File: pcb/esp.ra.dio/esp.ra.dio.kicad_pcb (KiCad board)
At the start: 2 copper layers, 75 x 28 mm, 34 parts, among them J1 A, J10 UART, J2 B, J3 C, J4 D, J5 START, J6 SELECT, J7 JOY, J8 USB_B_Micro, J9 BATTERY, Q1 BSS138, SW1 POWER, SW2 RESET, SW3 BOOT, U2 VCC, U3 RT9080-33GJ5

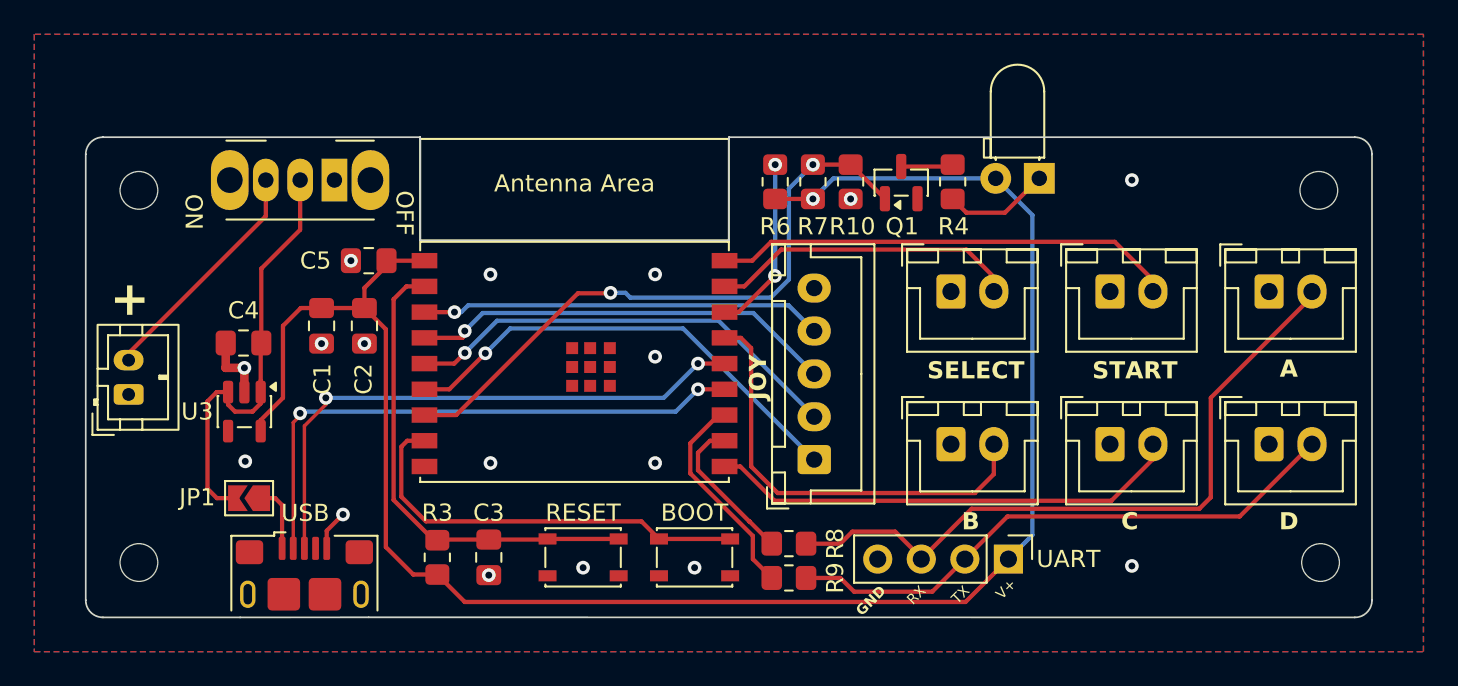
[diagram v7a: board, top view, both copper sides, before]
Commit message: Get rid of USB R0s
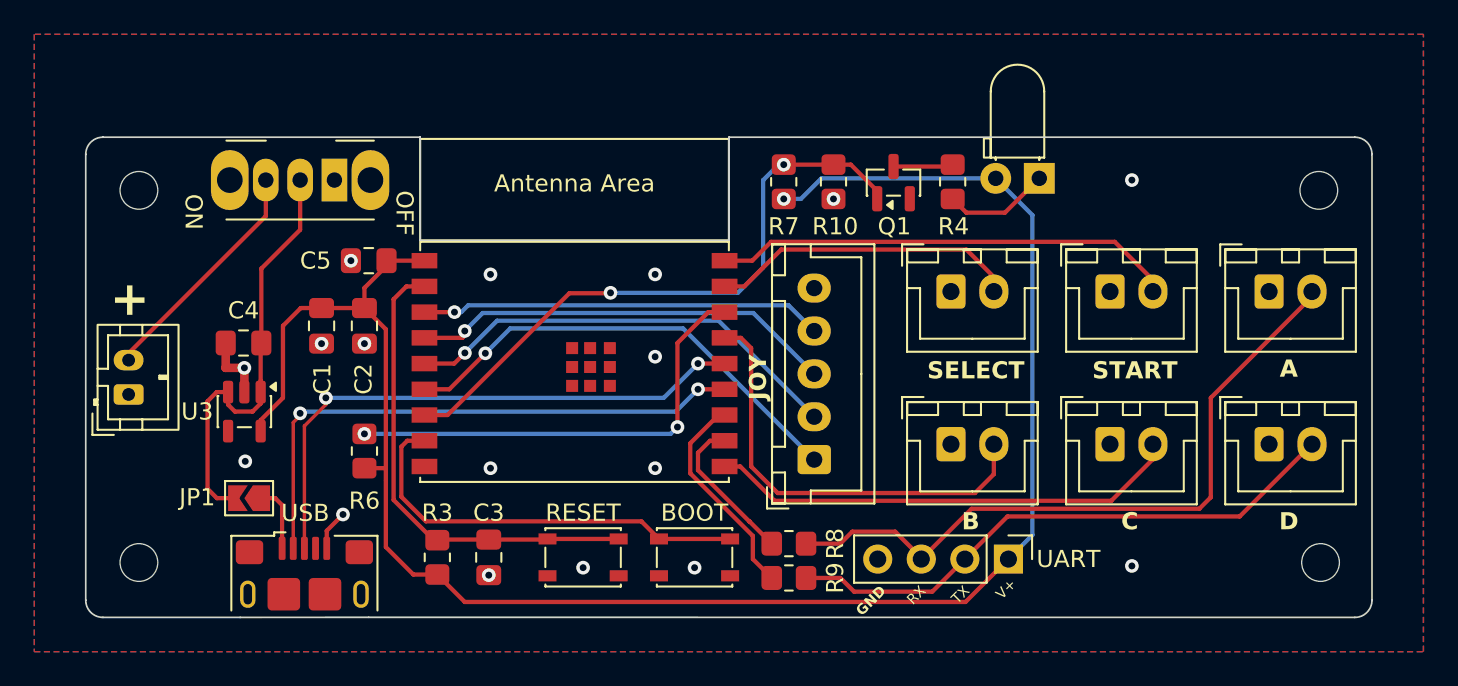
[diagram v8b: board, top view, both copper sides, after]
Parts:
- moved R6 28.6 mm to (54.2, 68.3)
- moved R7 1.70 mm to (78.7, 52.6)
- moved R10 1.00 mm to (81.6, 52.6)
- moved Q1 0.45 mm to (85.1, 52.6)
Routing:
- net /GPIO2: track 10.3 -> 26.8 mm
- net VCC: track 107.5 -> 108.3 mm
- net /ACTLED: track 37.2 -> 36.5 mm
